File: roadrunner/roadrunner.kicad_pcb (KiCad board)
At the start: 2 copper layers, 246.8 x 97.3 mm, 86 parts, among them J1 Battery_conn, J2 battery_conn_r, J4 niceview_left, J5 niceview_right, SW1 SW_Push, SW10 SW_Push, SW10_r1 SW_Push, SW11 SW_Push, SW11_r1 SW_Push, SW12 SW_Push, SW12_r1 SW_Push, SW13 SW_Push, SW13_r1 SW_Push, SW14 SW_Push, SW14_r1 SW_Push, SW15 SW_Push, SW15_r1 SW_Push, SW16 SW_Push, SW16_r1 SW_Push, SW17 SW_Push, SW17_r1 SW_Push, SW1_r1 SW_Push, SW2 SW_Push, SW2_r1 SW_Push, SW3 SW_Push, SW3_r1 SW_Push, SW4 SW_Push, SW4_r1 SW_Push, SW5 SW_Push, SW5_r1 SW_Push, SW6 SW_Push, SW6_r1 SW_Push, SW7 SW_Push, SW7_r1 SW_Push, SW8 SW_Push, SW8_r1 SW_Push, SW9 SW_Push, SW9_r1 SW_Push, U1 ProMicro-kbd, U2 ProMicro-kbd

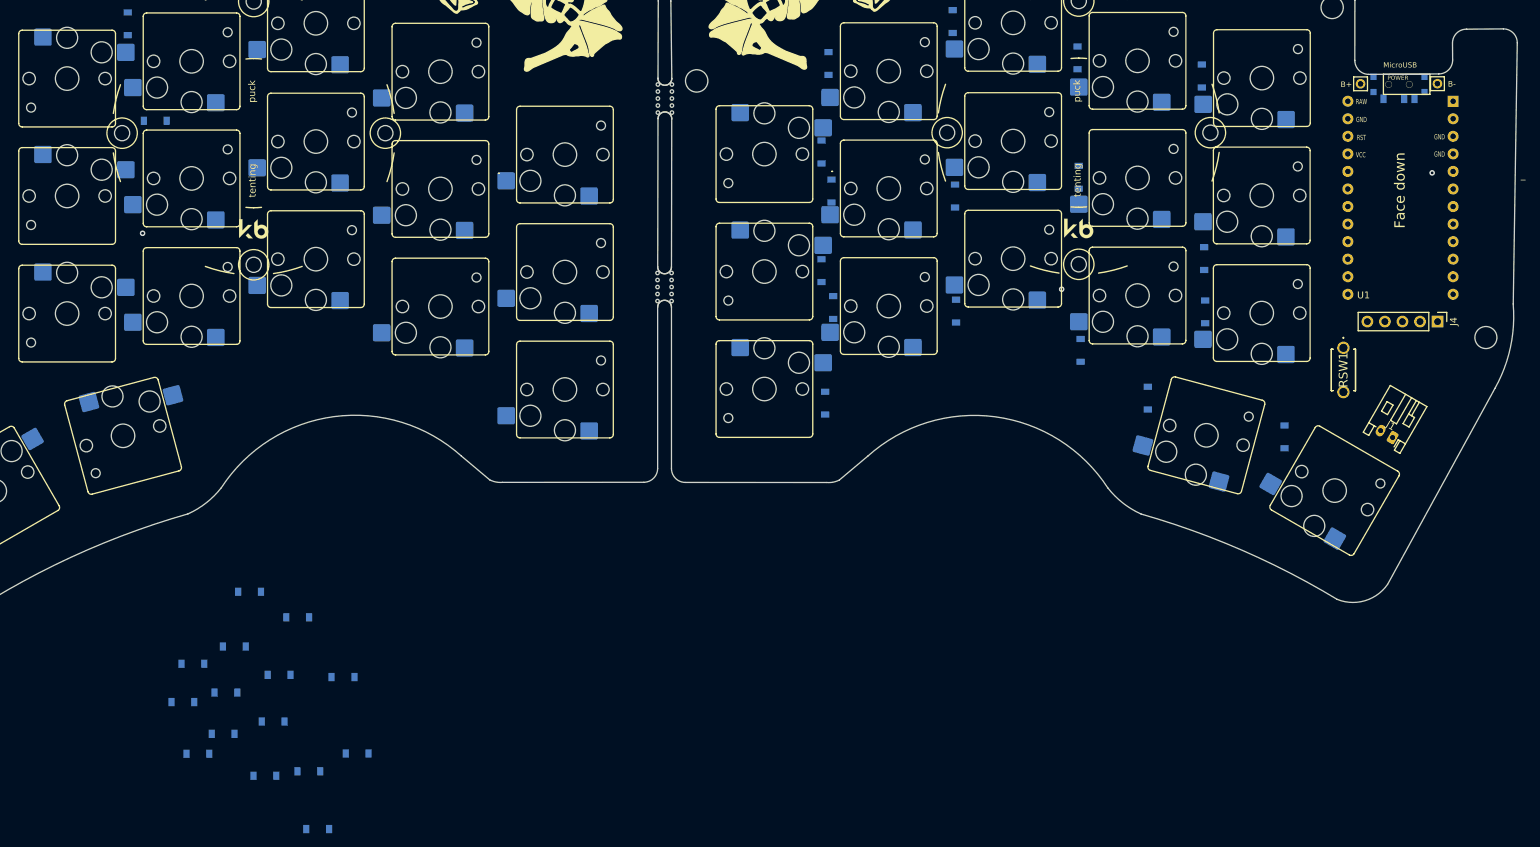
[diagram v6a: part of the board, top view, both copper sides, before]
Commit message: place diodes
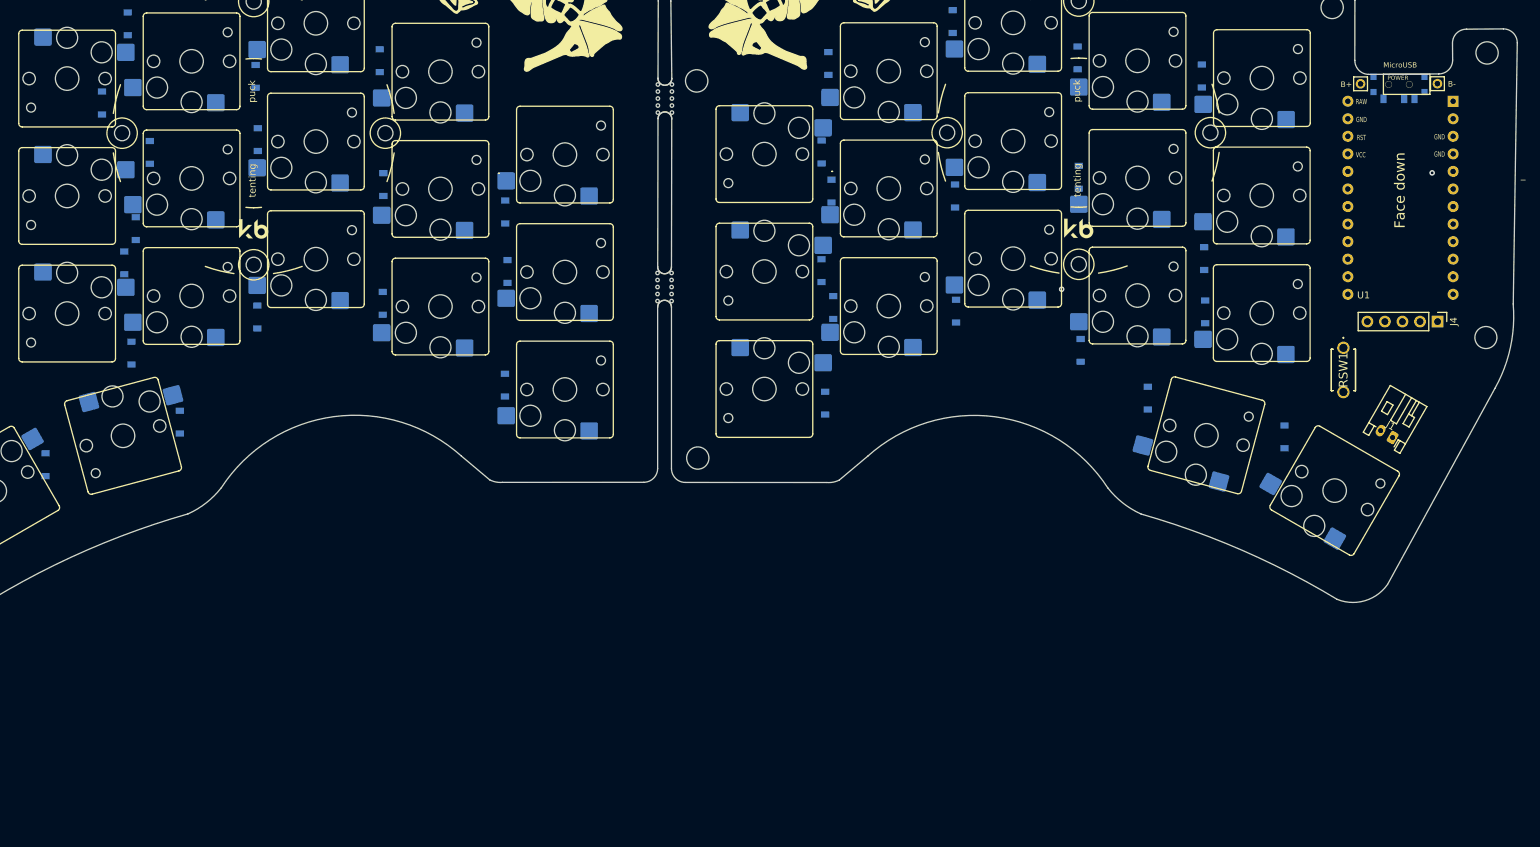
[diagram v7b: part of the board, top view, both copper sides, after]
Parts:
- moved D21 96.9 mm to (107.0, 46.8), turned to -90 degrees
- moved D28 86.6 mm to (70.0, 76.0), turned to -90 degrees
- moved D20 85.5 mm to (89.0, 49.0), turned to 90 degrees
- moved D26 82.4 mm to (107.5, 64.7), turned to -90 degrees
- moved D27 78.6 mm to (125.5, 77.2), turned to -90 degrees
- moved D22 74.6 mm to (125.1, 68.6), turned to 90 degrees
- moved D25 73.4 mm to (89.3, 58.2), turned to -90 degrees
- moved D23 70.6 mm to (73.7, 60.0), turned to -90 degrees
- moved D31 68.6 mm to (107.4, 81.9), turned to -90 degrees
- moved D24 68.4 mm to (71.7, 71.0), turned to 90 degrees
- moved D30 66.4 mm to (89.2, 83.8), turned to 90 degrees
- moved D29 51.1 mm to (71.0, 89.1), turned to 90 degrees
- moved D32 48.3 mm to (125.1, 93.7), turned to -90 degrees
- moved D34 48.1 mm to (78.0, 99.0), turned to 90 degrees
- moved D33 34.8 mm to (58.6, 105.2), turned to 90 degrees
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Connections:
- D20 pad 1: unconnected-(D20-Pad1) -> ROW0_r
- SW1 pad 1: unconnected-(SW1-Pad1) -> COL0
- SW1_r1 pad 1: unconnected-(SW1_r1-Pad1) -> COL4_r
- SW2_r1 pad 1: unconnected-(SW2_r1-Pad1) -> COL3_r
- SW3_r1 pad 1: unconnected-(SW3_r1-Pad1) -> COL2_r
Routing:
- net COL1_r: vias 1 -> 0
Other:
- outline, holes or cut-outs redrawn

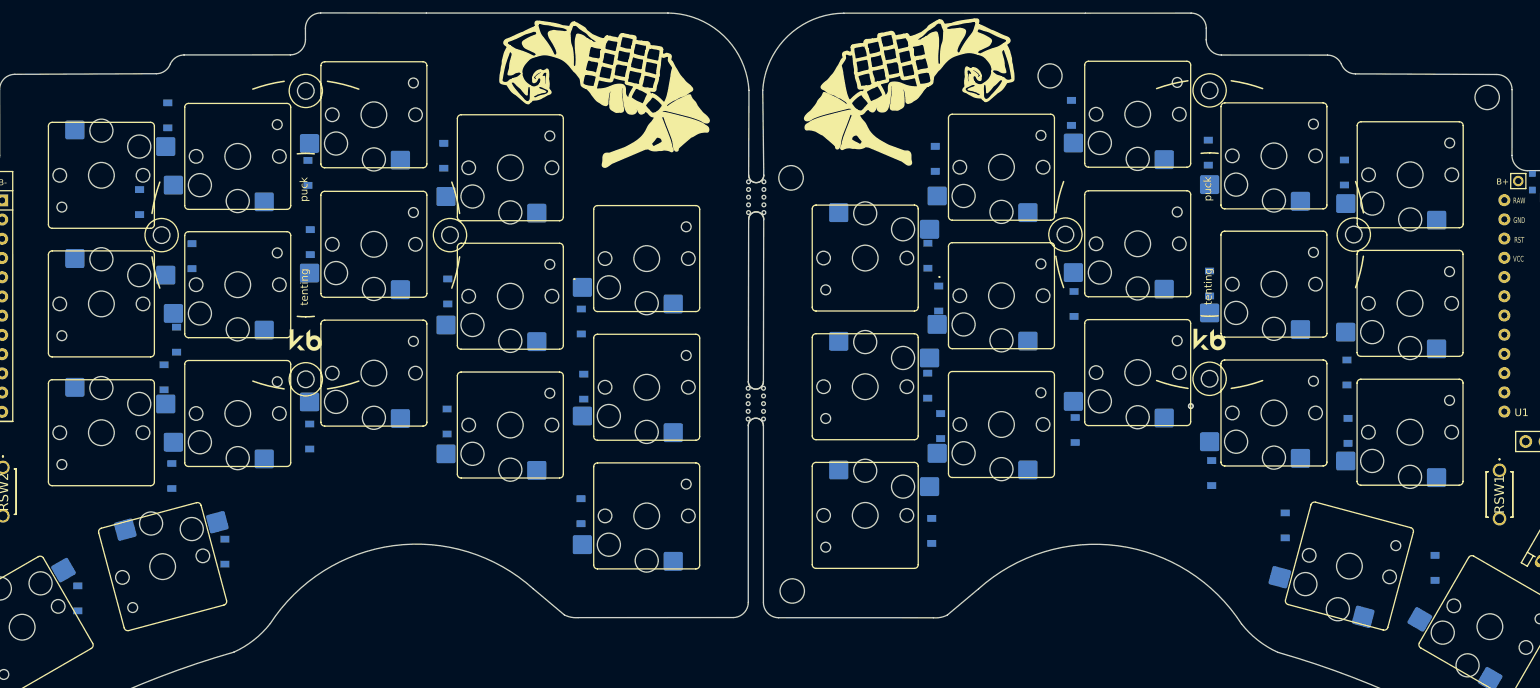
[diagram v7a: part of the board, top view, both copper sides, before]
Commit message: begin adding mouse
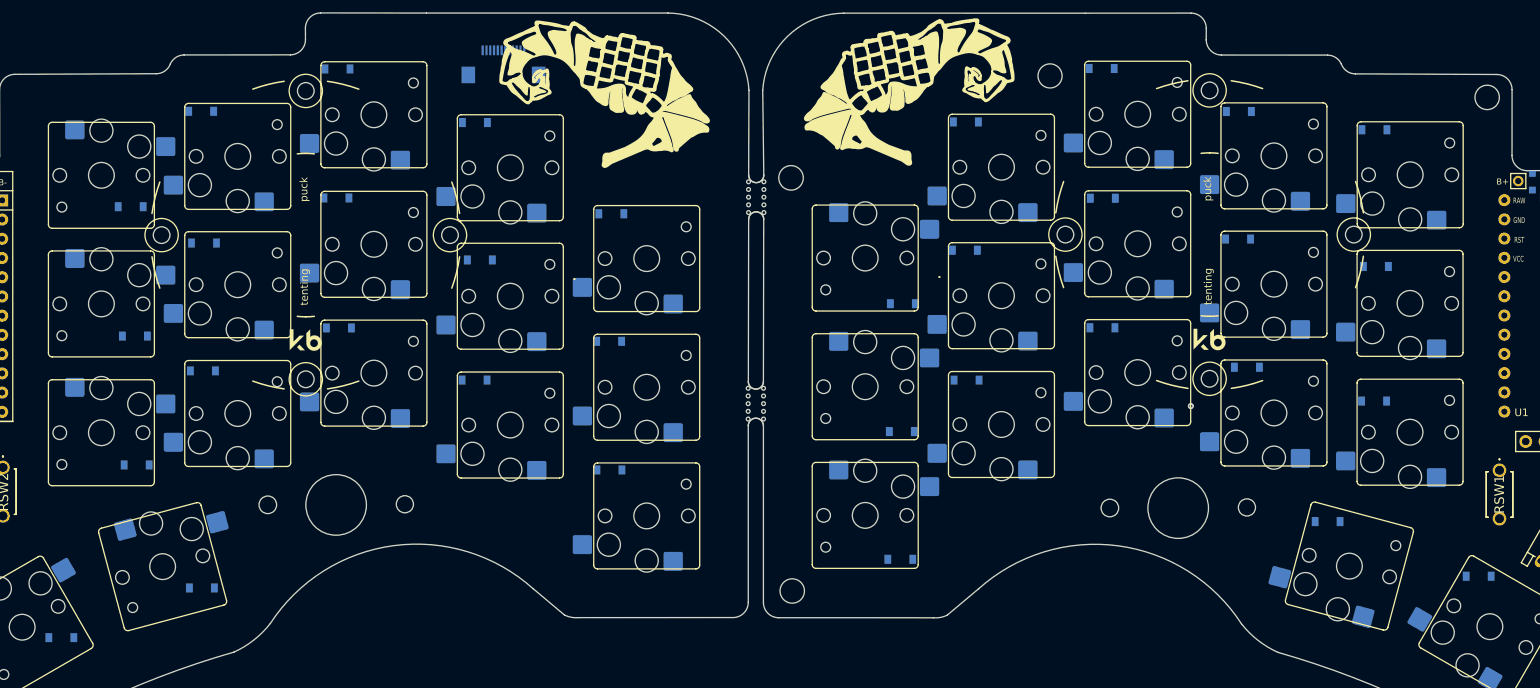
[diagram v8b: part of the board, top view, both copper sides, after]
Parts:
- added J3: Conn_01x12_Female, Connector_FFC-FPC:Hirose_FH12-12S-0.5SH_1x12-1MP_P0.50mm_Horizontal, B.Cu at (114.8, 34.7)
- moved D30 14.9 mm to (93.1, 69.5), turned to 0 degrees
- moved D22 14.8 mm to (129.1, 54.4), turned to 0 degrees
- moved D14 14.7 mm to (213.1, 74.7), turned to 0 degrees
- moved D10 14.5 mm to (230.1, 61.4), turned to 0 degrees
- moved D8 14.5 mm to (194.0, 52.4), turned to 0 degrees
- moved D20 14.3 mm to (92.9, 35.3), turned to 0 degrees
- moved D13 14.0 mm to (194.0, 69.5), turned to 0 degrees
- moved D3 7.10 mm to (193.9, 35.2), turned to 0 degrees
- moved D9 6.98 mm to (211.9, 57.8), turned to 0 degrees
- moved D5 6.90 mm to (229.9, 43.3), turned to 0 degrees
- moved D27 6.86 mm to (128.8, 71.3), turned to 0 degrees
- moved D25 6.79 mm to (92.8, 52.3), turned to 0 degrees
- moved D4 6.77 mm to (212.0, 40.9), turned to 0 degrees
- moved D32 6.63 mm to (128.8, 88.2), turned to 0 degrees
- moved D31 6.57 mm to (111.0, 76.4), turned to 0 degrees
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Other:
- outline, holes or cut-outs redrawn
